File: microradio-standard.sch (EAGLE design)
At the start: 13 parts, among them T1 NPN (ECB)

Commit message: added lib
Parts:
- C1, C2, C5: device capacitor-wima:C5/3 -> microradio-standard:C5/3
- C3: device rcl:CPOL-USB45181C -> microradio-standard:CPOL-USB45181A
- C4: device c-trimm:C-TRIMM3008 -> microradio-standard:C-TRIMM3008
- JP1, JP2: device pinhead:PINHD-1X2 -> microradio-standard:PINHD-1X2
- JP3: device pinhead:PINHD-1X1 -> microradio-standard:PINHD-1X1
- L1: device rcl:L-US0204/5 -> microradio-standard:L-US0204/5
- R1, R2, R3: device resistor:R-US_0204/7 -> microradio-standard:R-US_0207/7
- T1: device transistor:-NPN-TO92 -> microradio-standard:-NPN-TO92-BCE
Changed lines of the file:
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@@
 </classes>
 <parts>
-<part name="C1" library="capacitor-wima" deviceset="C" device="5/3" value="0.01uF"/>
-<part name="C2" library="capacitor-wima" deviceset="C" device="5/3" value="10pF"/>
-<part name="L1" library="rcl" deviceset="L-US" device="0204/5"/>
-<part name="R1" library="resistor" deviceset="R-US_" device="0204/7" value="470"/>
-<part name="R2" library="resistor" deviceset="R-US_" device="0204/7" value="10K"/>
-<part name="R3" library="resistor" deviceset="R-US_" device="0204/7" value="27K"/>
+<part name="C1" library="microradio-standard" deviceset="C" device="5/3" value="0.01uF"/>
+<part name="C2" library="microradio-standard" deviceset="C" device="5/3" value="10pF"/>
+<part name="L1" library="microradio-standard" deviceset="L-US" device="0204/5"/>
+<part name="R1" library="microradio-standard" deviceset="R-US_" device="0207/7" value="470"/>
+<part name="R2" library="microradio-standard" deviceset="R-US_" device="0207/7" value="10K"/>
+<part name="R3" library="microradio-standard" deviceset="R-US_" device="0207/7" value="27K"/>
 <part name="FRAME1" library="frames" deviceset="DINA5_L" device=""/>
-<part name="C3" library="rcl" deviceset="CPOL-US" device="B45181C" value="33uF"/>
-<part name="C4" library="c-trimm" deviceset="C-TRIMM" device="3008" value="10pF"/>
-<part name="T1" library="transistor" deviceset="*-NPN-" device="TO92" value="NPN (ECB)"/>
-<part name="JP1" library="pinhead" deviceset="PINHD-1X2" device="" value="audio_in"/>
-<part name="JP2" library="pinhead" deviceset="PINHD-1X2" device="" value="BATT"/>
-<part name="JP3" library="pinhead" deviceset="PINHD-1X1" device="" value="RF"/>
-<part name="C5" library="capacitor-wima" deviceset="C" device="5/3" value="0.01uF"/>
-<part name="GND1" library="supply1" deviceset="GND" device=""/>
-<part name="GND2" library="supply1" deviceset="GND" device=""/>
+<part name="C3" library="microradio-standard" deviceset="CPOL-US" device="B45181A" value="33uF"/>
+<part name="C4" library="microradio-standard" deviceset="C-TRIMM" device="3008" value="10pF"/>
+<part name="T1" library="microradio-standard" deviceset="*-NPN-" device="TO92-BCE" value="NPN (ECB)"/>
+<part name="JP1" library="microradio-standard" deviceset="PINHD-1X2" device="" value="audio_in"/>
+<part name="JP2" library="microradio-standard" deviceset="PINHD-1X2" device="" value="BATT"/>
+<part name="JP3" library="microradio-standard" deviceset="PINHD-1X1" device="" value="RF"/>
+<part name="C5" library="microradio-standard" deviceset="C" device="5/3" value="0.01uF"/>
+<part name="GND1" library="microradio-standard" deviceset="GND" device=""/>
+<part name="GND2" library="microradio-standard" deviceset="GND" device=""/>
 </parts>
 <sheets>

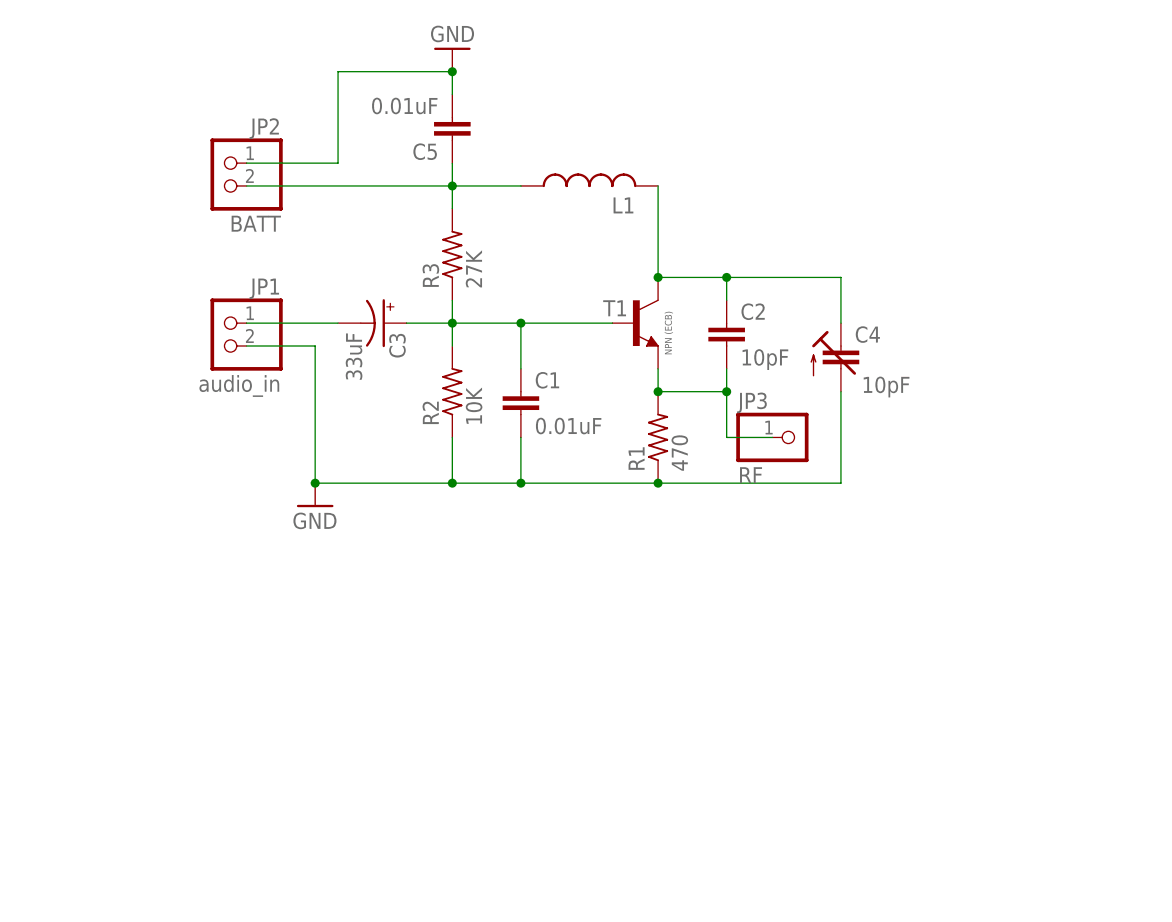
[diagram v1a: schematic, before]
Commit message: moving to smd
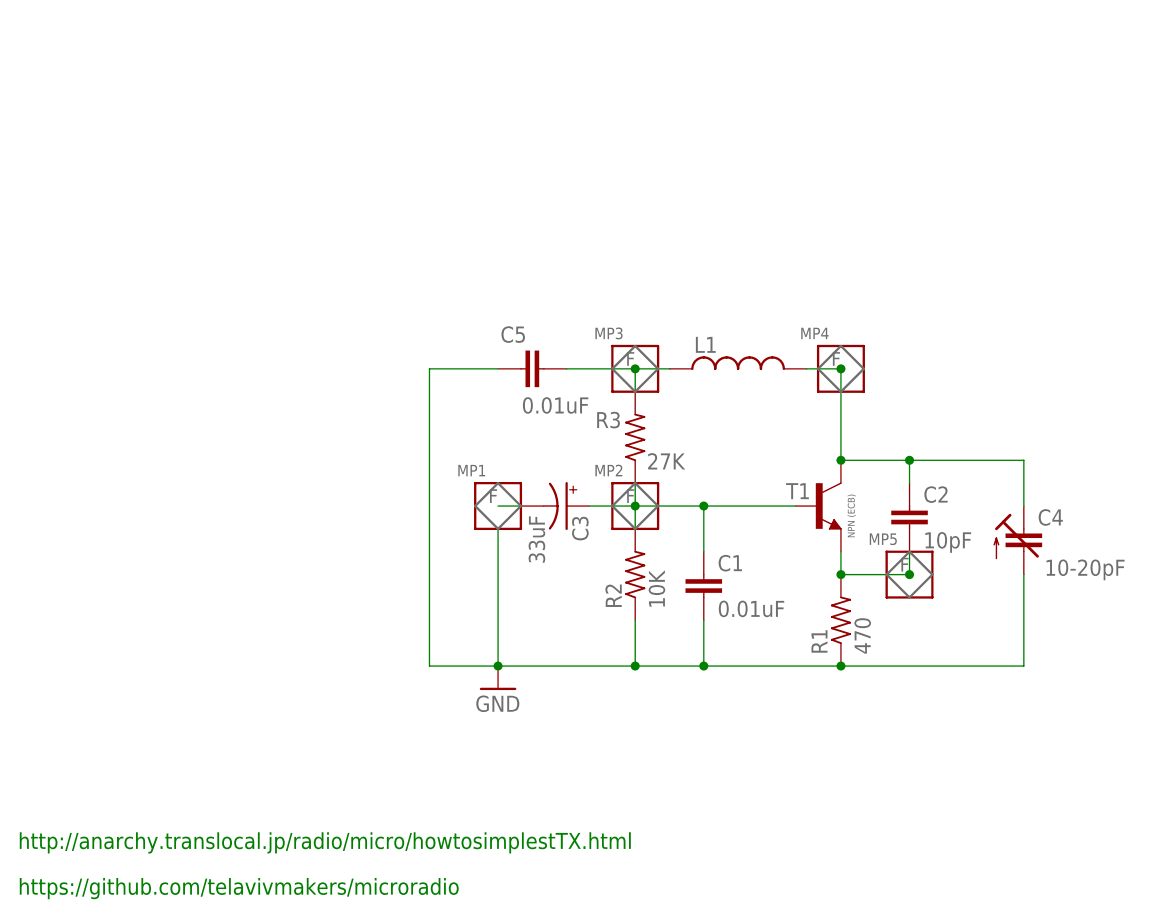
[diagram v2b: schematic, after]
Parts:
- removed JP1: audio_in, microradio-standard:PINHD-1X2
- removed JP2: BATT, microradio-standard:PINHD-1X2
- removed JP3: RF, microradio-standard:PINHD-1X1
- added MP1, MP2, MP3, MP4, MP5: MICROSTRIPMI, microradio-standard:MICROSTRIPMI
- C4: value 10pF -> 10-20pF
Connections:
- removed net N$5: C2.1, C4.E, L1.2, T1.C
- new net N$6: C2.1, C4.E, L1.2, MP4.E, T1.C
- net GND: no longer JP1.2, JP2.1
- net N$1: now also MP1.E; no longer JP1.1
- net N$2: now also MP5.E; no longer JP3.1
- net N$3: now also MP3.E; no longer JP2.2
- net N$4: now also MP2.E
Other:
- note added: "http://anarchy.translocal.jp/radio/micro/howtosimplestTX.html"
- note added: "https://github.com/telavivmakers/microradio"
- moved on the sheet: C1, C2, C3, C4, C5, L1, R1, R2, R3, T1

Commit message: smd version, is this legfit microstrip?
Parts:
- C1, C5: device microradio-standard:C5/3 -> microradio-standard:C
- C3: device microradio-standard:CPOL-USB45181A -> microradio-standard:CPOL-US153CLV-0405
- R1, R2, R3: device microradio-standard:R-US_0207/7 -> microradio-standard:R-US_R1206
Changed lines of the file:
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@@
 </classes>
 <parts>
-<part name="C1" library="microradio-standard" deviceset="C" device="5/3" value="0.01uF"/>
+<part name="C1" library="microradio-standard" deviceset="C" device="" value="0.01uF"/>
 <part name="C2" library="microradio-standard" deviceset="C" device="5/3" value="10pF"/>
 <part name="L1" library="microradio-standard" deviceset="L-US" device="0204/5"/>
-<part name="R1" library="microradio-standard" deviceset="R-US_" device="0207/7" value="470"/>
-<part name="R2" library="microradio-standard" deviceset="R-US_" device="0207/7" value="10K"/>
-<part name="R3" library="microradio-standard" deviceset="R-US_" device="0207/7" value="27K"/>
+<part name="R1" library="microradio-standard" deviceset="R-US_" device="R1206" value="470"/>
+<part name="R2" library="microradio-standard" deviceset="R-US_" device="R1206" value="10K"/>
+<part name="R3" library="microradio-standard" deviceset="R-US_" device="R1206" value="27K"/>
 <part name="FRAME1" library="frames" deviceset="DINA5_L" device=""/>
-<part name="C3" library="microradio-standard" deviceset="CPOL-US" device="B45181A" value="33uF"/>
+<part name="C3" library="microradio-standard" deviceset="CPOL-US" device="153CLV-0405" value="33uF"/>
 <part name="C4" library="microradio-standard" deviceset="C-TRIMM" device="3008" value="10-20pF"/>
 <part name="T1" library="microradio-standard" deviceset="*-NPN-" device="TO92-BCE" value="NPN (ECB)"/>
-<part name="C5" library="microradio-standard" deviceset="C" device="5/3" value="0.01uF"/>
+<part name="C5" library="microradio-standard" deviceset="C" device="" value="0.01uF"/>
 <part name="GND1" library="microradio-standard" deviceset="GND" device=""/>
 <part name="MP2" library="microradio-standard" deviceset="MICROSTRIP" device="MI"/>
